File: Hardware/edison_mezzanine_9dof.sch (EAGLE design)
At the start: 31 parts, among them U1 LSM9DS0

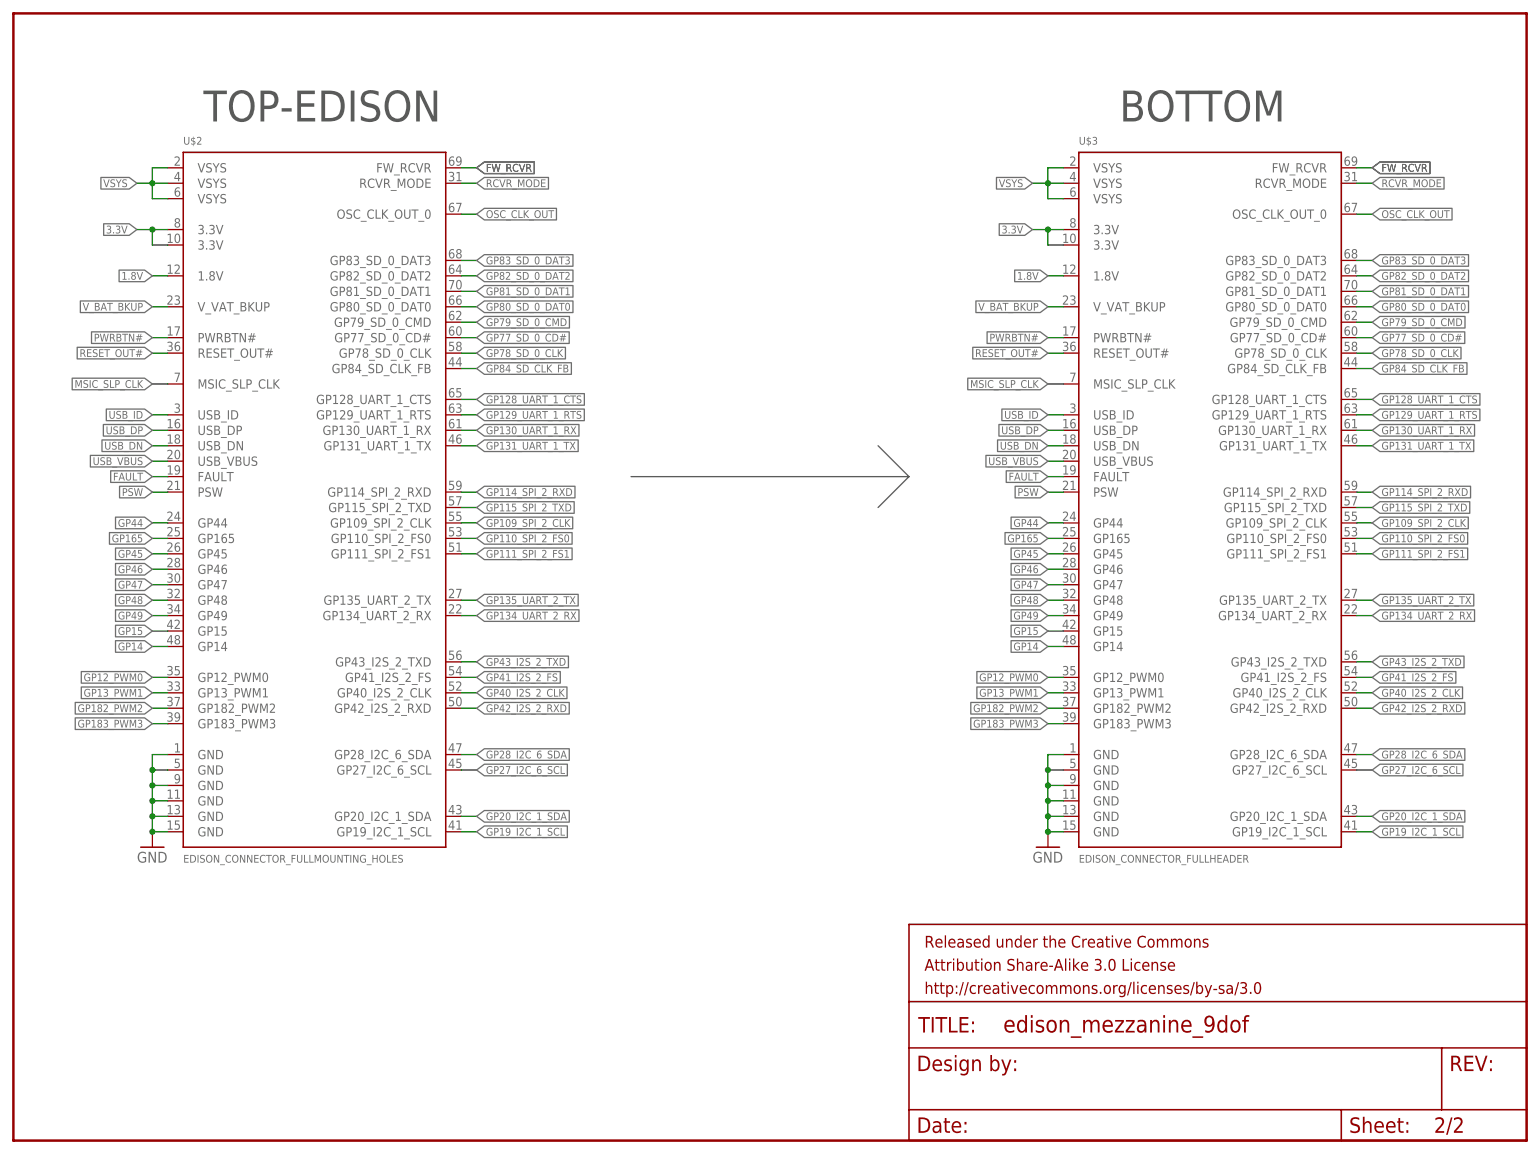
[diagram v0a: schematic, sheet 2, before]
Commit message: Updated to new template. Initial component placement.
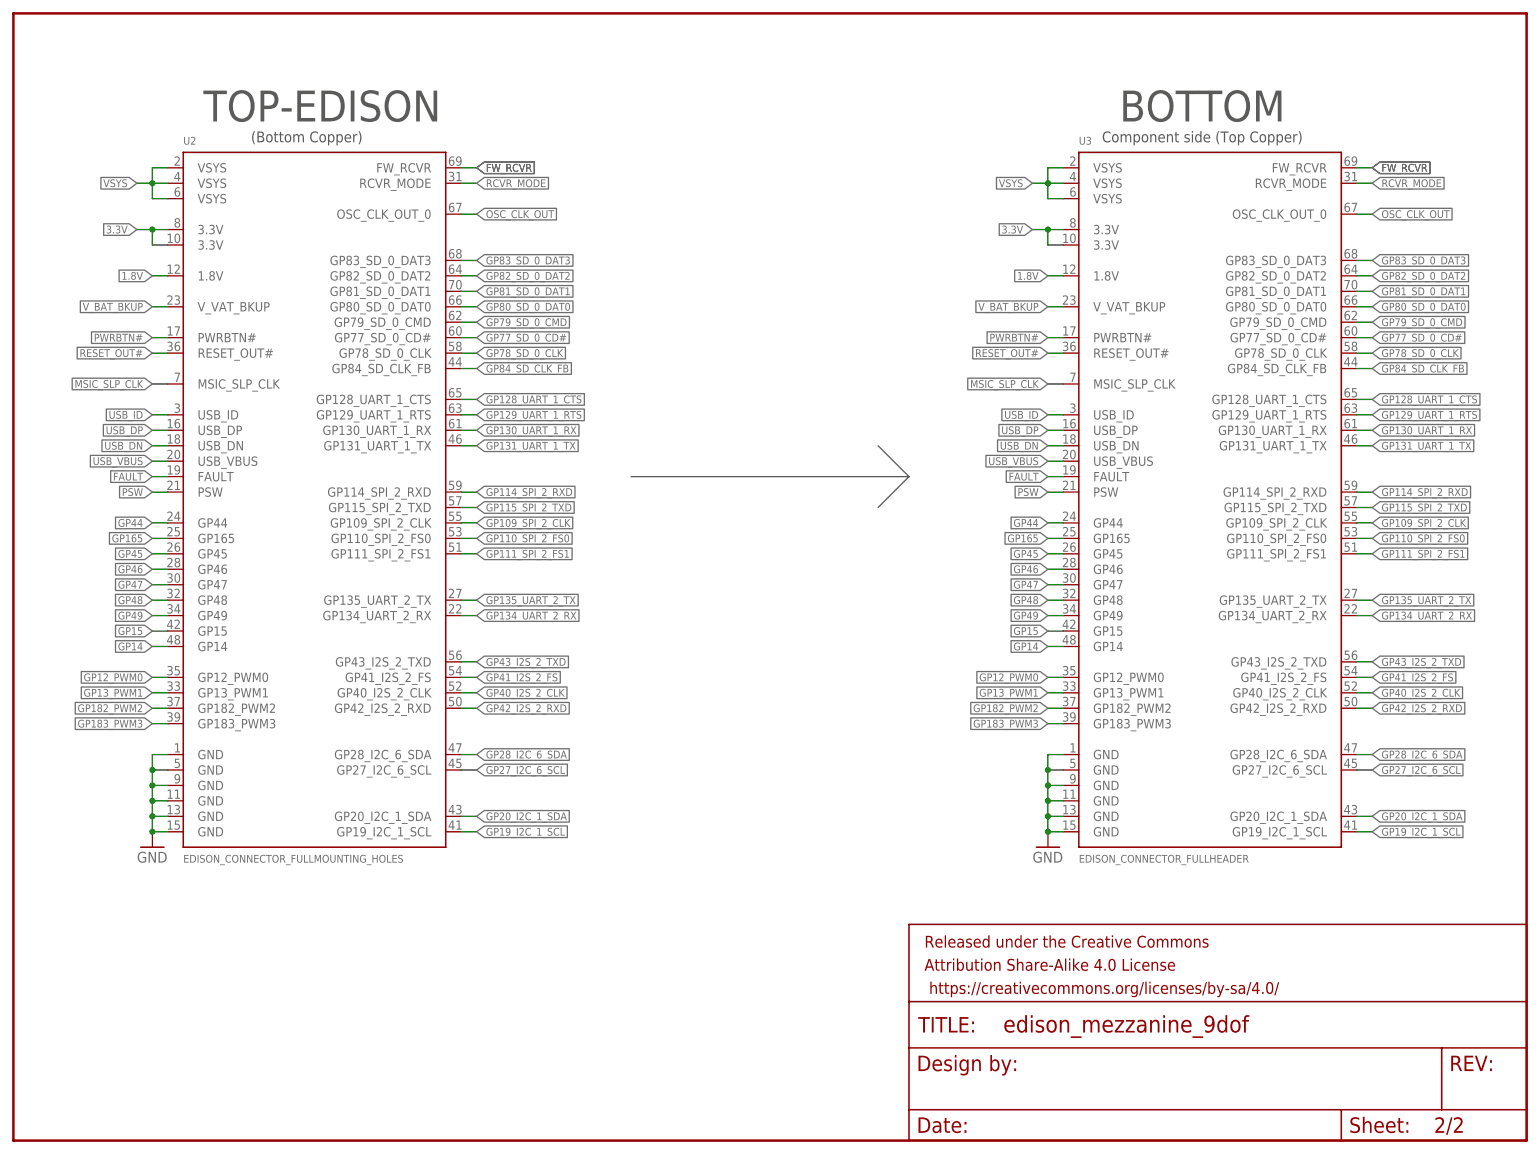
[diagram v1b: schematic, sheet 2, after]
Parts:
- renumbered U$2 to U2, U$3 to U3
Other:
- note added: "(Bottom Copper)"
- note added: "Component side (Top Copper)"

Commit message: v01 board layout complete
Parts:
- removed FRAME2: FRAME-LETTER, SparkFun-Aesthetics:FRAME-LETTER
- added LOGO1: SFE_LOGO_FLAME.3_INCH, SparkFun-Aesthetics:SFE_LOGO_FLAME.3_INCH
- added SJ15: JUMPER-PAD-3-NOYES_SILK, SparkFun-Passives:JUMPER-PAD-3-NOYES_SILK
- C3: PROD_ID (none) -> CAP-11330
- SJ1, SJ2, SJ3: value (none) -> JUMPER-PAD-3-NC_BY_PASTE; device SparkFun-Passives:SOLDERJUMPER_2WAYS -> SparkFun-Passives:JUMPER-PAD-3-NC_BY_PASTE
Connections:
- net GND: now also SJ15.2
- net SDO_G: now also SJ15.3
- net SDO_XM: now also SJ15.1
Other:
- note added: "v01"
- note removed: "v10"
- moved on the sheet: C1, C2, C3, C4, SJ10, SJ11, SJ12, SJ13, SJ14, SJ4, SJ5, SJ6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

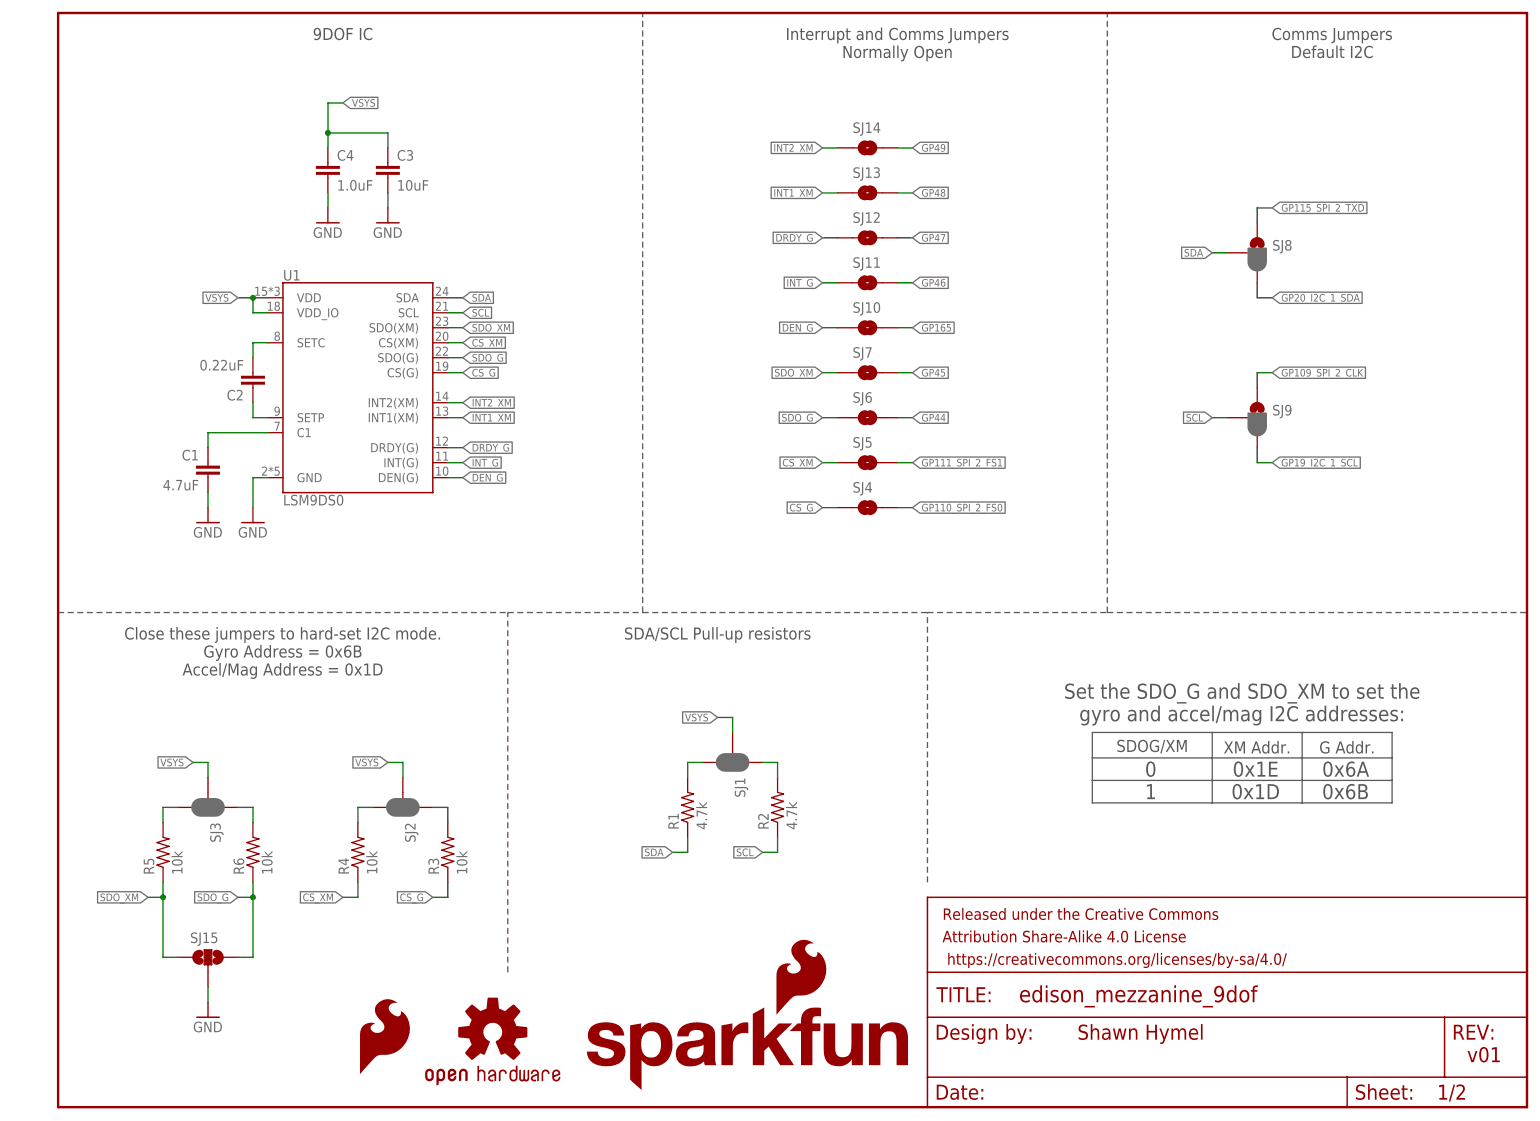
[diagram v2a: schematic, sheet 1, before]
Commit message: Added LDO
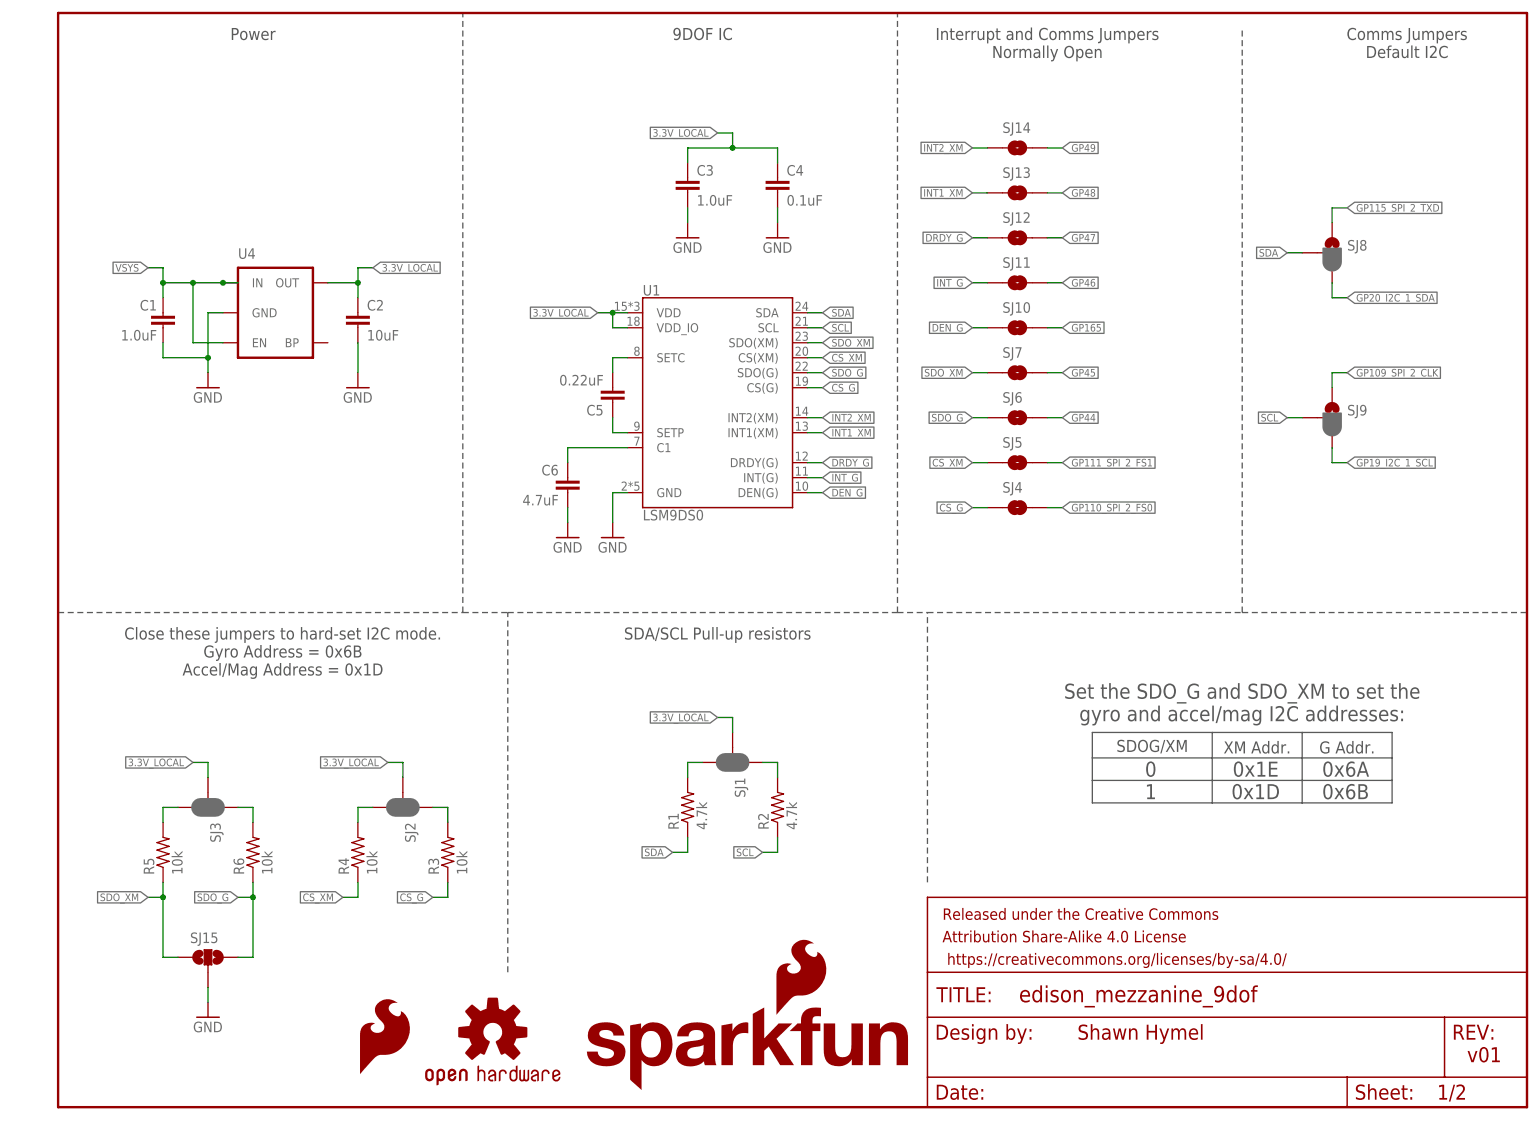
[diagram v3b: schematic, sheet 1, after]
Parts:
- added C5: 0.22uF, SparkFun-Capacitors:0.22UF-25V-10%(0603)
- added C6: 4.7uF, SparkFun-Capacitors:4.7UF-6.3V-10%(0603)0603
- added U4: (no value), SparkFun-PowerIC:MIC52053.3V
- C1: value 4.7uF -> 1.0uF; device SparkFun-Capacitors:4.7UF-6.3V-10%(0603)0603 -> SparkFun-Capacitors:1.0UF-16V-10%(0603)
- C2: value 0.22uF -> 10uF; device SparkFun-Capacitors:0.22UF-25V-10%(0603) -> SparkFun-Capacitors:CAP0805; PROD_ID (none) -> CAP-11330
- C3: value 10uF -> 1.0uF; device SparkFun-Capacitors:CAP0805 -> SparkFun-Capacitors:1.0UF-16V-10%(0603); PROD_ID CAP-11330 -> (none)
- C4: value 1.0uF -> 0.1uF; device SparkFun-Capacitors:1.0UF-16V-10%(0603) -> SparkFun-Capacitors:0.1UF-25V(+80/-20%)(0603)
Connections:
- new net 3.3V_LOCAL: C2.1, C3.1, C4.1, SJ1.2, SJ2.2, SJ3.2, U1.VDD, U1.VDD_IO, U4.OUT
- net GND: now also C2.2, C6.2, U4.GND
- net N$1: now also C5.1; no longer C2.1
- net N$2: now also C5.2; no longer C2.2
- net N$3: now also C6.1; no longer C1.1
- net VSYS: now also C1.1, U4.EN, U4.IN; no longer C3.1, C4.1, SJ1.2, SJ2.2, SJ3.2, U1.VDD, U1.VDD_IO
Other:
- note added: "Power"
- moved on the sheet: C1, C2, C3, C4, SJ10, SJ11, SJ12, SJ13, SJ14, SJ4, SJ5, SJ6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
